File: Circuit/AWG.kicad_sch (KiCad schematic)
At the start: 25 parts, among them J1 Power, J2 Pump 1, J3 Pump 2, J4 Pump 3, J5 WL1, M1 Fan_3pin, M2 Fan_3pin, Q1 RFP30N06LE, Q2 RFP30N06LE, SW1 Switch, U2 LCD-016N002L

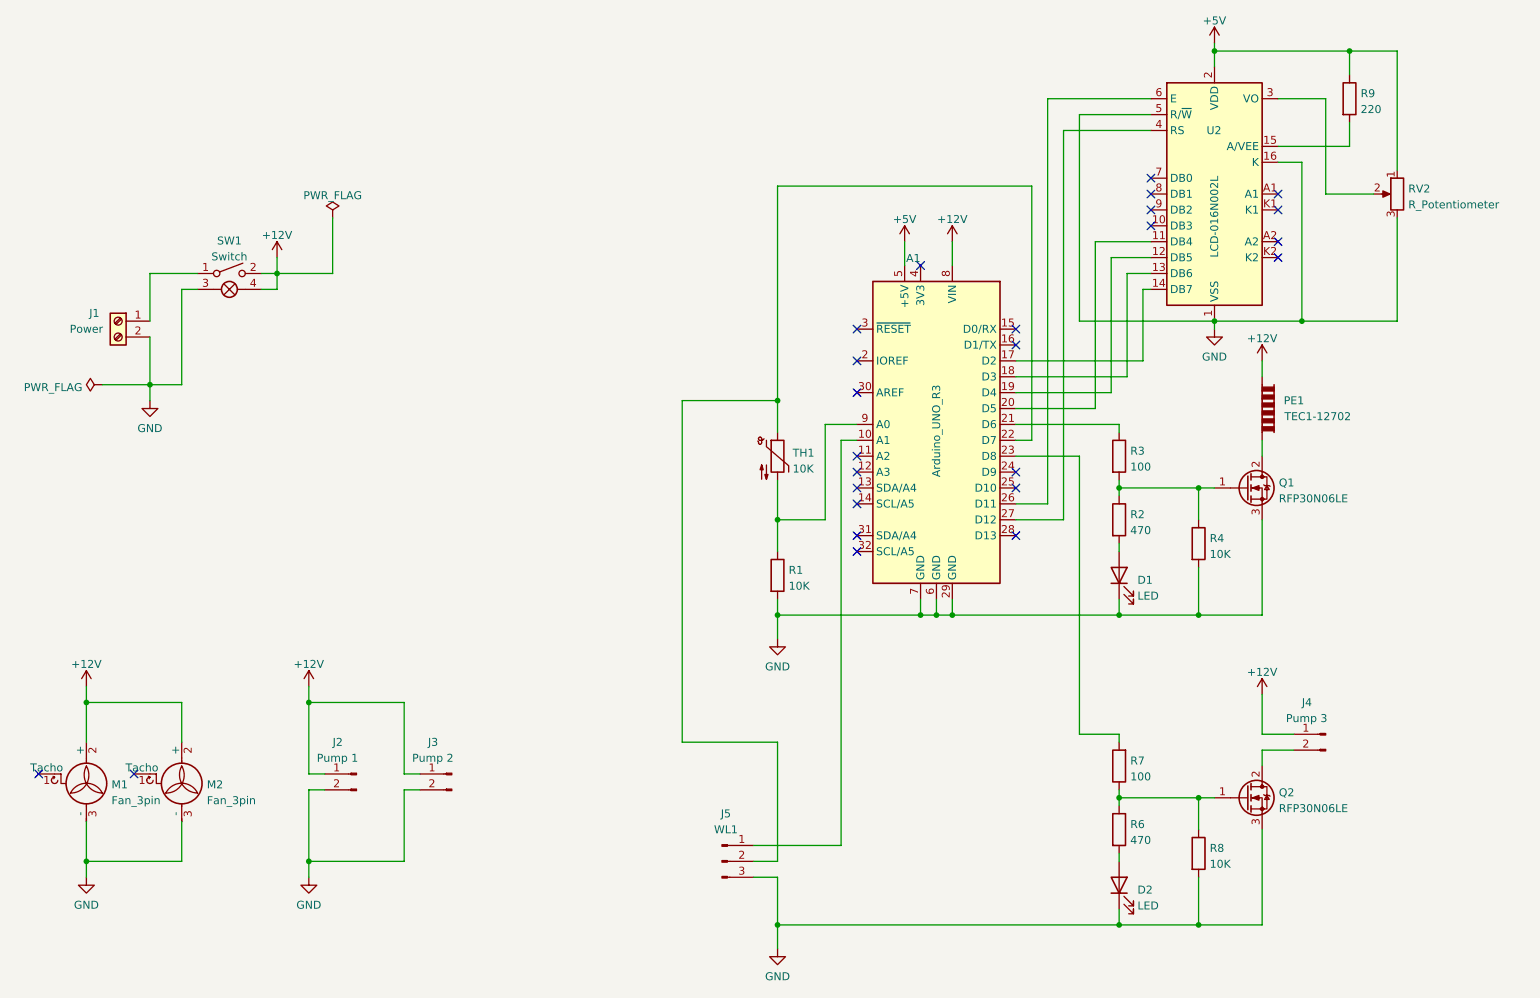
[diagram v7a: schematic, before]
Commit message: [Circuit] Change to use I2C screen
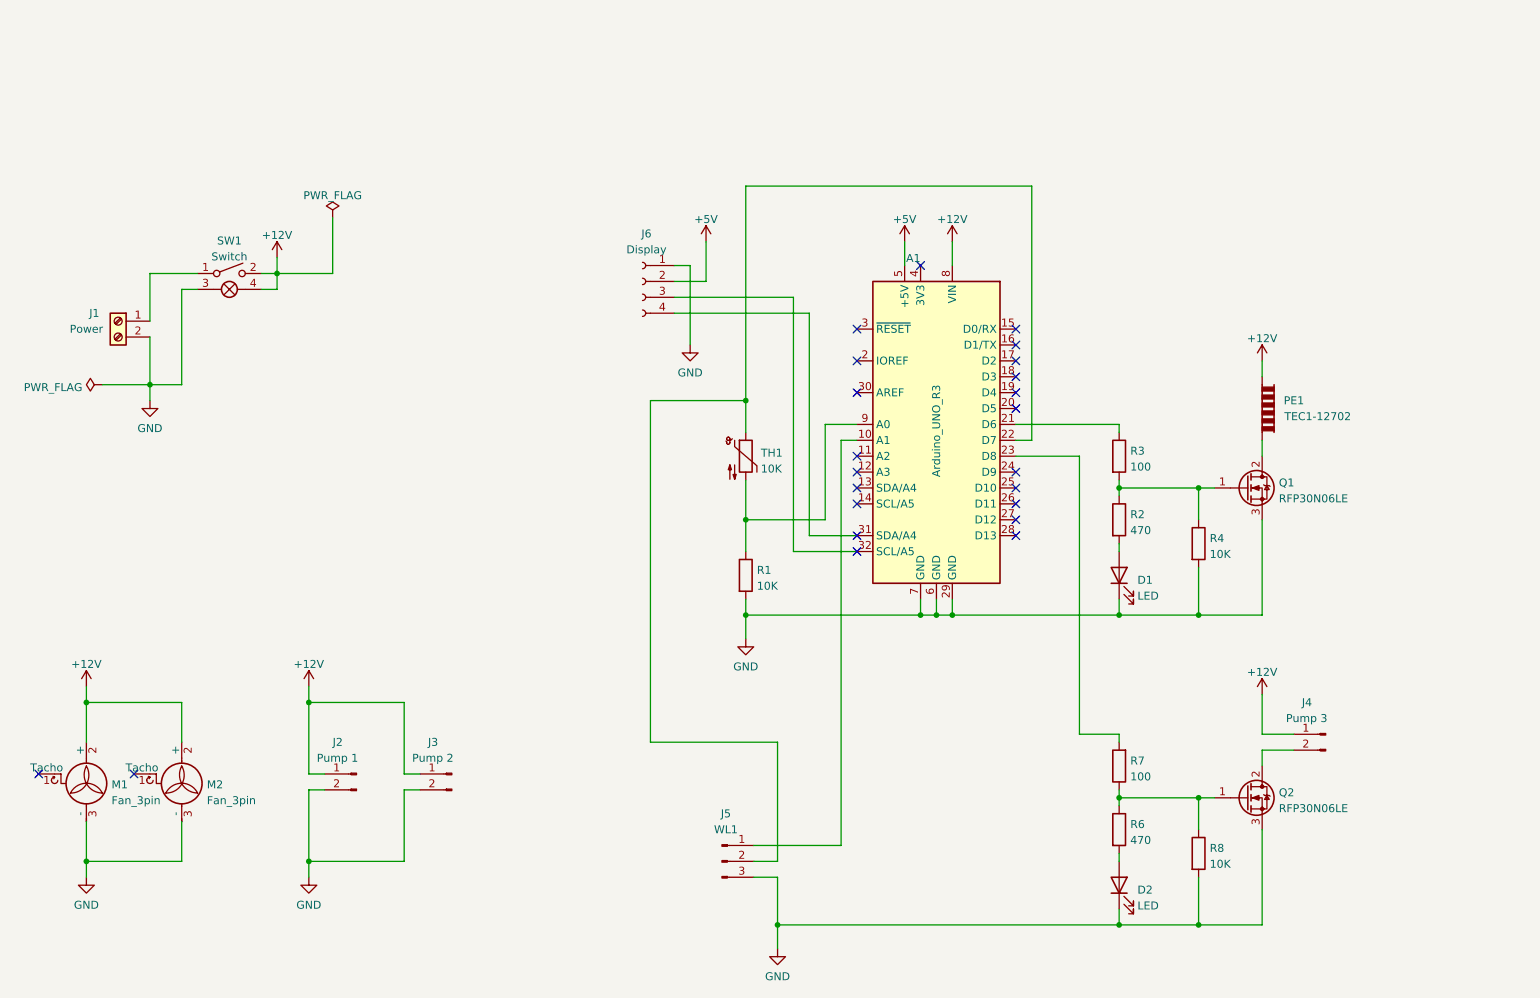
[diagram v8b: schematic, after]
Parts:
- removed R9: 220, Resistor_THT:R_Axial_DIN0207_L6.3mm_D2.5mm_P7.62mm_Horizontal, symbol Device:R
- removed RV2: R_Potentiometer, symbol Device:R_Potentiometer
- removed U2: LCD-016N002L, Display:LCD-016N002L, symbol Display_Character:LCD-016N002L
- added J6: Display, Connector_PinSocket_2.54mm:PinSocket_1x04_P2.54mm_Vertical, symbol Connector:Conn_01x04_Female
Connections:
- net +5V: now also J6.2 (Pin_2)
- net GND: now also J6.1 (Pin_1)
- net at A1.31 (SDA/A4): now also J6.4 (Pin_4)
- net at A1.32 (SCL/A5): now also J6.3 (Pin_3)
- no-connect marks 25 -> 23
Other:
- moved on the sheet: R1, TH1
